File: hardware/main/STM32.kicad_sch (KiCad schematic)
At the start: 36 parts, among them U201 REF3430QDGKRQ1, U202 STM32L431RCTx

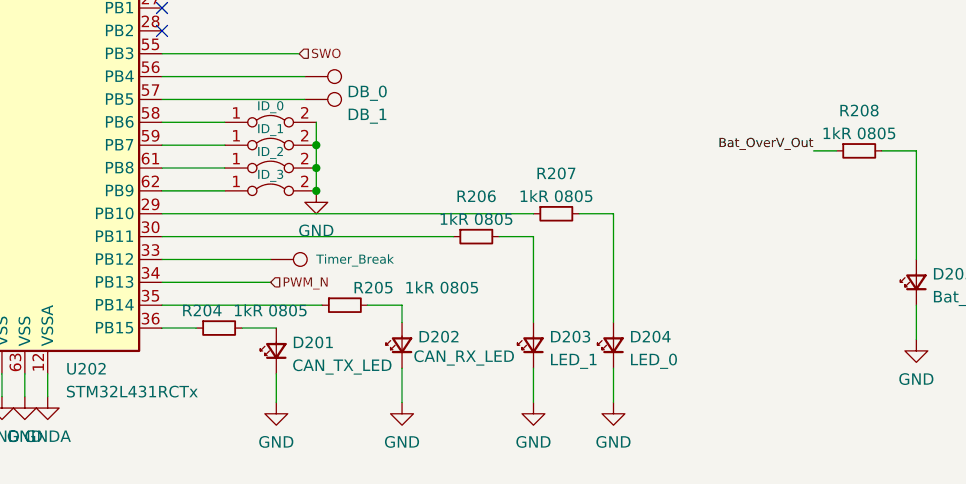
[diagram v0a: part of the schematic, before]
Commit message: Schematics: Change LED order for better pcb routing
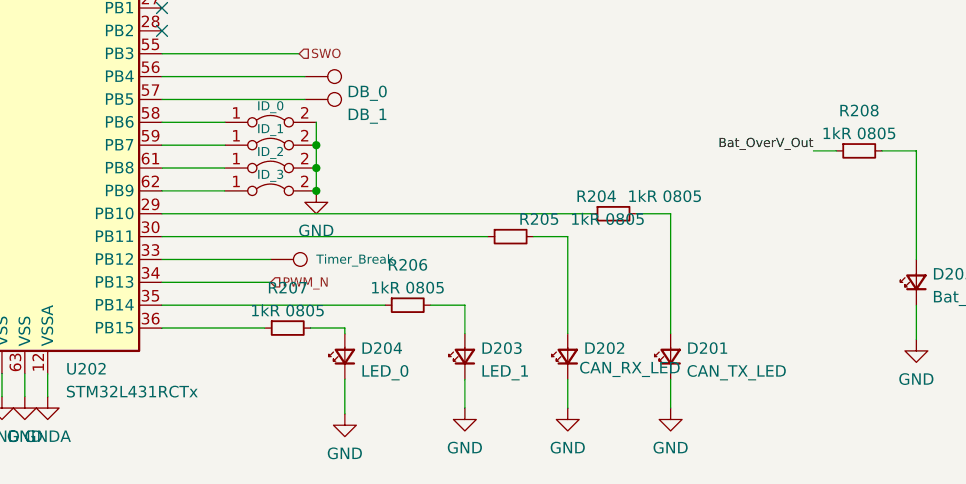
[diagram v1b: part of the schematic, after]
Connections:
- net at R205.1: now also U202.30 (PB11); no longer U202.35 (PB14)
- net at R207.1: now also U202.36 (PB15); no longer U202.29 (PB10)
- net at R206.1: now also U202.35 (PB14); no longer U202.30 (PB11)
- net at R204.1: now also U202.29 (PB10); no longer U202.36 (PB15)
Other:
- moved on the sheet: D201, D202, D203, D204, R204, R205, R206, R207

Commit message: Layout: WIP updating control
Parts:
- removed JP202: Enable Voltage Reference, Zenite:SolderJumper-2_P0.5mm_Open_TrianglePad0.5x0.5mm, symbol Jumper:Jumper_2_Bridged
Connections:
- net 5VA is gone; now on net 5V: C201.2, C202.2, U201.1 (ENABLE), U201.8 (VIN)
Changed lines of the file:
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@@
-    (stroke (width 0) (type default) (color 0 0 0 0))
-  )
-  (wire (pts (xy 246.38 22.86) (xy 250.053 22.86))
     (stroke (width 0) (type default) (color 0 0 0 0))
   )
@@
     (stroke (width 0) (type default) (color 0 0 0 0))
   )
-  (wire (pts (xy 232.41 22.86) (xy 236.22 22.86))
+  (wire (pts (xy 232.41 22.86) (xy 250.053 22.86))
     (stroke (width 0) (type default) (color 0 0 0 0))
   )
@@
     (pin "1")
   )
-  (symbol (lib_id "Jumper:Jumper_2_Bridged") (at 241.3 22.86 0) (unit 1)
-    (in_bom yes) (on_board yes) (fields_autoplaced)
-    (property "Reference" "JP202" (id 0) (at 241.3 18.5252 0))
-    (property "Value" "Enable Voltage Reference" (id 1) (at 241.3 21.0621 0))
-    (property "Footprint" "Zenite:SolderJumper-2_P0.5mm_Open_TrianglePad0.5x0.5mm" (id 2) (at 241.3 22.86 0)
-      (effects (font (size 1.27 1.27)) hide)
-    )
-    (property "Datasheet" "~" (id 3) (at 241.3 22.86 0)
-      (effects (font (size 1.27 1.27)) hide)
-    )
-    (pin "1")
-    (pin "2")
-  )
   (symbol (lib_id "Jumper:Jumper_2_Bridged") (at 240.03 50.165 0) (unit 1)

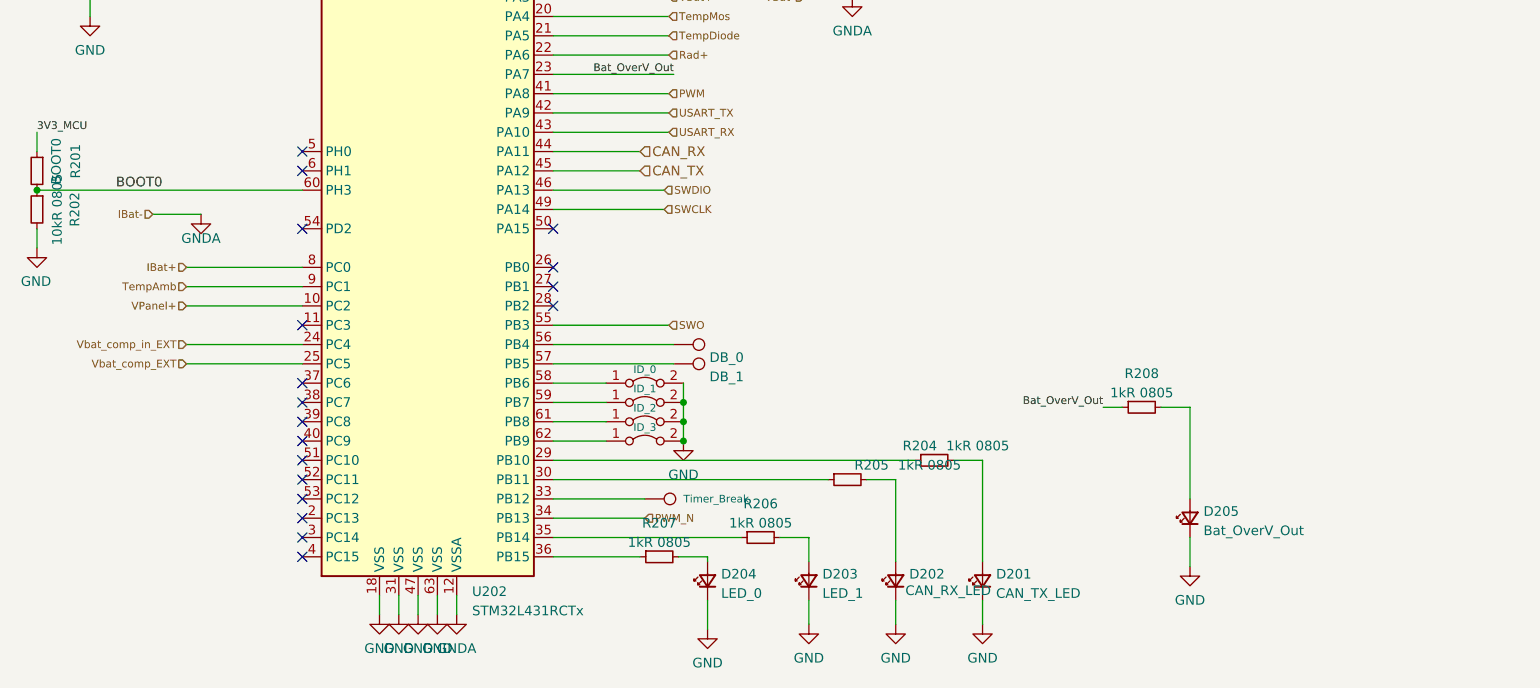
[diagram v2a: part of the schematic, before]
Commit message: Layout: Designing thermal dissipation and optimizing control
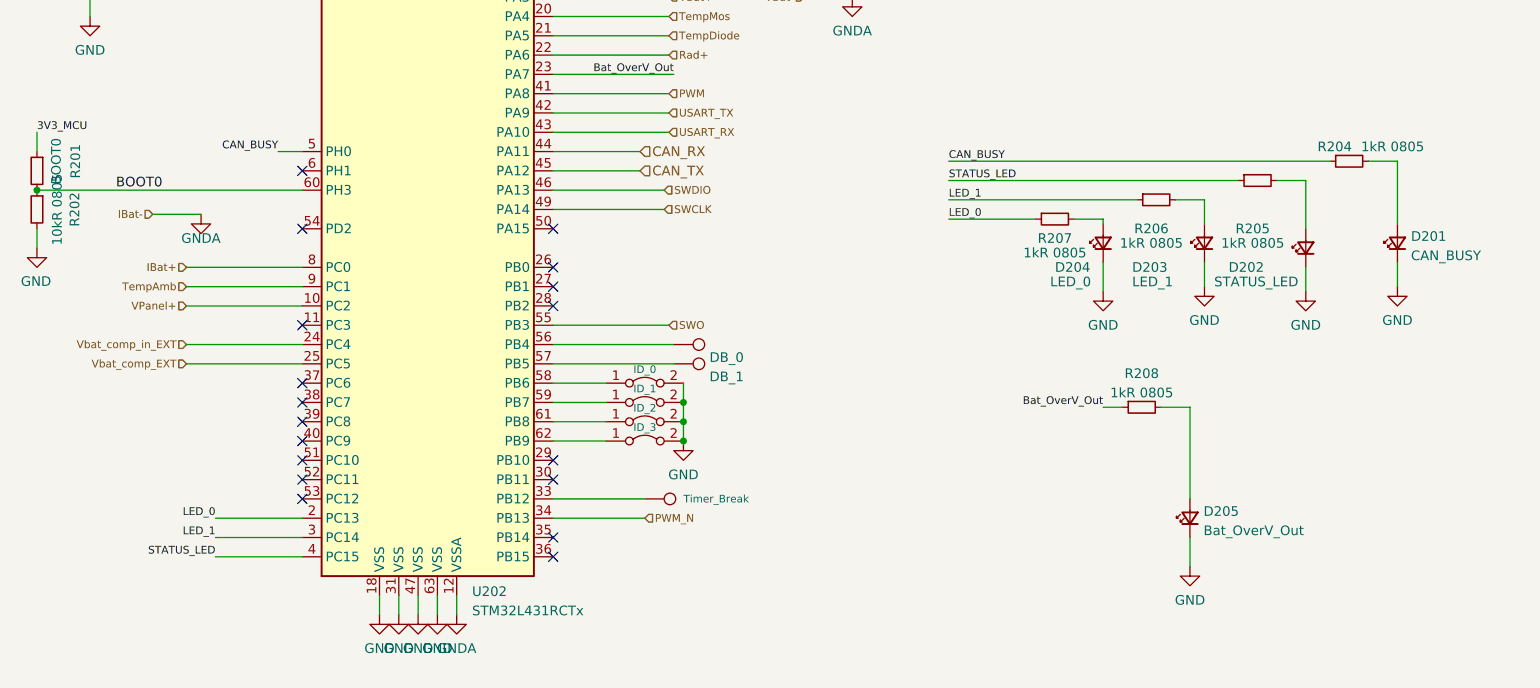
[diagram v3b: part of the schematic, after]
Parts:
- D201: value CAN_TX_LED -> CAN_BUSY
- D202: value CAN_RX_LED -> STATUS_LED
- JP203: footprint Jumper:SolderJumper-3_P2.0mm_Open_TrianglePad1.0x1.5mm -> Zenite:SolderJumper-3_P0.5mm_Open_TrianglePad0.8x0.5mm
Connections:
- net at U202.30 (PB11): no longer R205.1
- net at U202.36 (PB15): no longer R207.1
- net at U202.35 (PB14): no longer R206.1
- net at U202.29 (PB10): no longer R204.1
- net LED_0: now reaches U202.2 (PC13)
- net LED_0: now also R207.1
- net LED_1: now reaches U202.3 (PC14)
- net LED_1: now also R206.1
- net STATUS_LED: now reaches U202.4 (PC15)
- net STATUS_LED: now also R205.1
- net CAN_BUSY: now reaches U202.5 (PH0)
- net CAN_BUSY: now also R204.1
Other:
- moved on the sheet: D201, D202, D203, D204, R204, R205, R206, R207

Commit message: Layout: Connect all unconected nets, and fix all DRC errors
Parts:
- JP201, JP204, JP205, JP206, JP207: footprint Zenite:SolderJumper-2_P0.5mm_Open_TrianglePad0.5x0.5mm -> Zenite:SolderJumper-2_P0.5mm_Open_TrianglePad0.8x0.5mm
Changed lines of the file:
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@@
       (effects (font (size 1 1)))
     )
-    (property "Footprint" "Zenite:SolderJumper-2_P0.5mm_Open_TrianglePad0.5x0.5mm" (id 2) (at 167.64 142.24 0)
+    (property "Footprint" "Zenite:SolderJumper-2_P0.5mm_Open_TrianglePad0.8x0.5mm" (id 2) (at 167.64 142.24 0)
       (effects (font (size 1.27 1.27)) hide)
     )
@@
     (property "Reference" "JP201" (id 0) (at 240.03 45.8302 0))
     (property "Value" "Enable Stm32 Supply" (id 1) (at 240.03 48.3671 0))
-    (property "Footprint" "Zenite:SolderJumper-2_P0.5mm_Open_TrianglePad0.5x0.5mm" (id 2) (at 240.03 50.165 0)
+    (property "Footprint" "Zenite:SolderJumper-2_P0.5mm_Open_TrianglePad0.8x0.5mm" (id 2) (at 240.03 50.165 0)
       (effects (font (size 1.27 1.27)) hide)
     )
@@
       (effects (font (size 1 1)))
     )
-    (property "Footprint" "Zenite:SolderJumper-2_P0.5mm_Open_TrianglePad0.5x0.5mm" (id 2) (at 167.64 137.16 0)
+    (property "Footprint" "Zenite:SolderJumper-2_P0.5mm_Open_TrianglePad0.8x0.5mm" (id 2) (at 167.64 137.16 0)
       (effects (font (size 1.27 1.27)) hide)
     )
@@
       (effects (font (size 1 1)))
     )
-    (property "Footprint" "Zenite:SolderJumper-2_P0.5mm_Open_TrianglePad0.5x0.5mm" (id 2) (at 167.64 139.7 0)
+    (property "Footprint" "Zenite:SolderJumper-2_P0.5mm_Open_TrianglePad0.8x0.5mm" (id 2) (at 167.64 139.7 0)
       (effects (font (size 1.27 1.27)) hide)
     )
@@
       (effects (font (size 1 1)))
     )
-    (property "Footprint" "Zenite:SolderJumper-2_P0.5mm_Open_TrianglePad0.5x0.5mm" (id 2) (at 167.64 134.62 0)
-      (effects (font (size 1.27 1.27)) hide)
-    )
+    (property "Footprint" "Zenite:SolderJumper-2_P0.5mm_Open_TrianglePad0.8x0.5mm" (id 2) (at 167.64 134.62 0)
+      (effects (font (size 1.27 1.27)) hide)
+    )

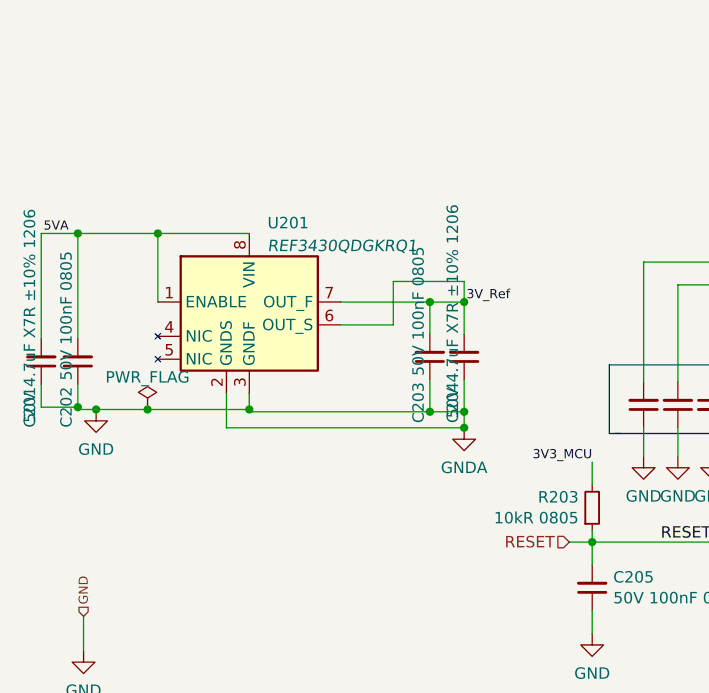
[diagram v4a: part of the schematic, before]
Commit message: layout: Separating analogical power nets
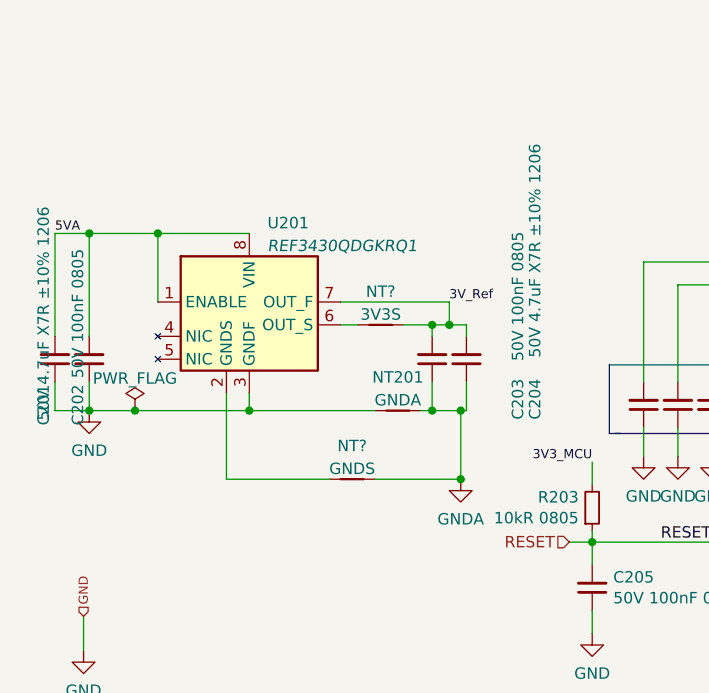
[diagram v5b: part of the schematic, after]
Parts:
- added NT201: GNDA, Resistor_SMD:R_0201_0603Metric, symbol Device:NetTie_2
- added NT?: 3V3S, Resistor_SMD:R_0201_0603Metric, symbol Device:NetTie_2
- added NT?: GNDS, Resistor_SMD:R_0201_0603Metric, symbol Device:NetTie_2
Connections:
- net 3V_Ref: now also NT?.1; no longer U201.6 (OUT_S)
- net GND: now also NT201.2; no longer C203.1, C204.1, C211.1, U201.2 (GNDS), U202.12 (VSSA), U202.15 (PA1)
- new net: NT?.2, U201.6 (OUT_S)
- new net: NT?.2, U201.2 (GNDS)
- new net GNDA: C203.1, C204.1, C211.1, NT201.1, NT?.1, U202.12 (VSSA), U202.15 (PA1)
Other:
- moved on the sheet: C201, C202

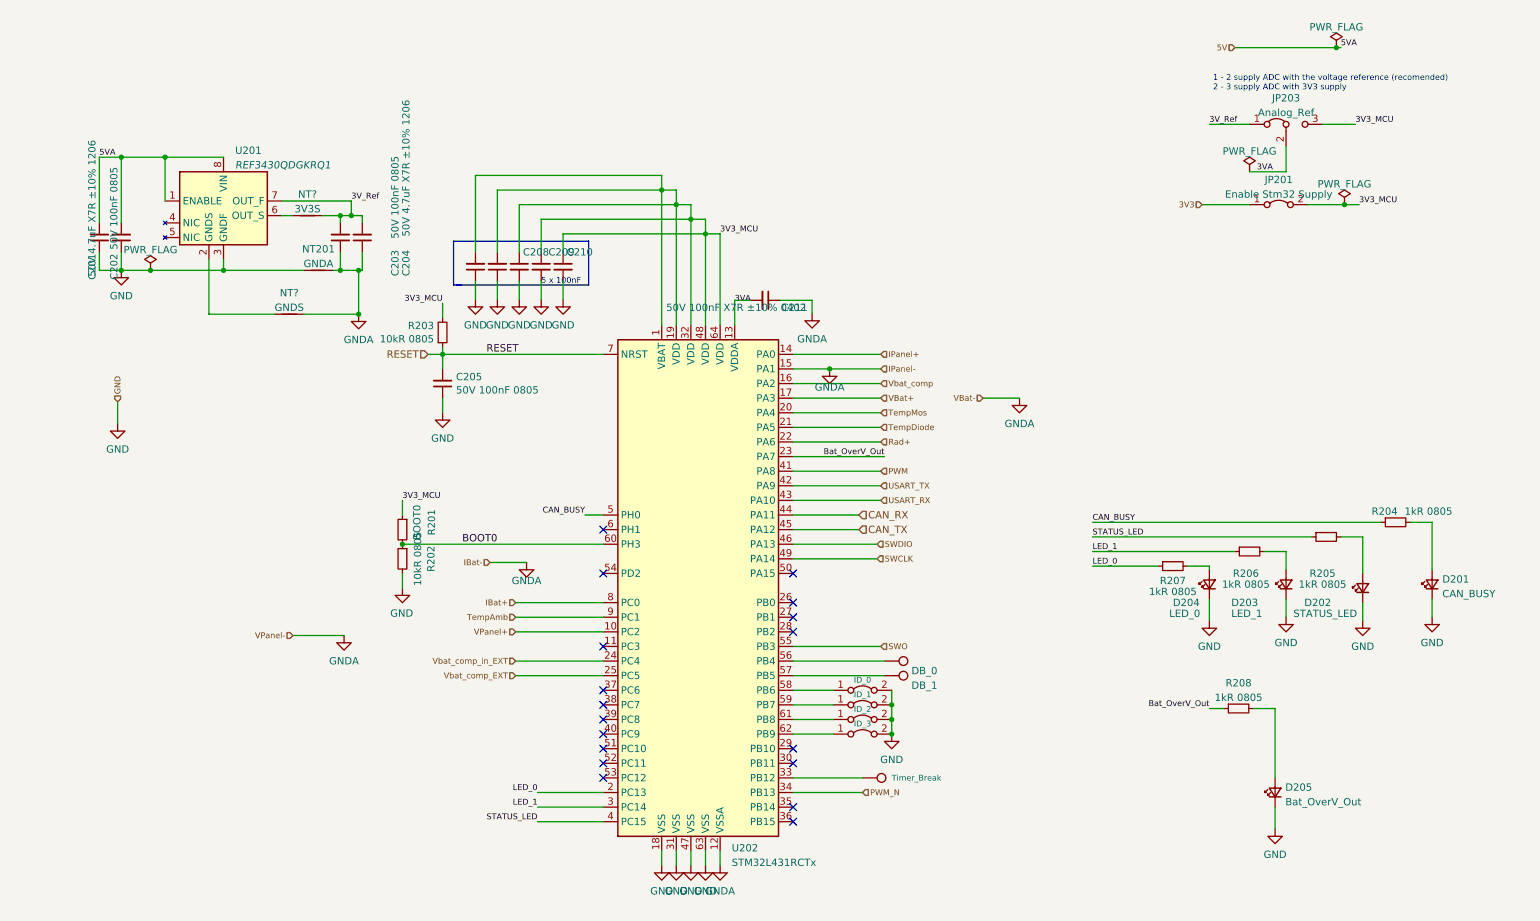
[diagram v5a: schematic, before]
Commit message: Layout: Place components and route analog, supplies and CAN
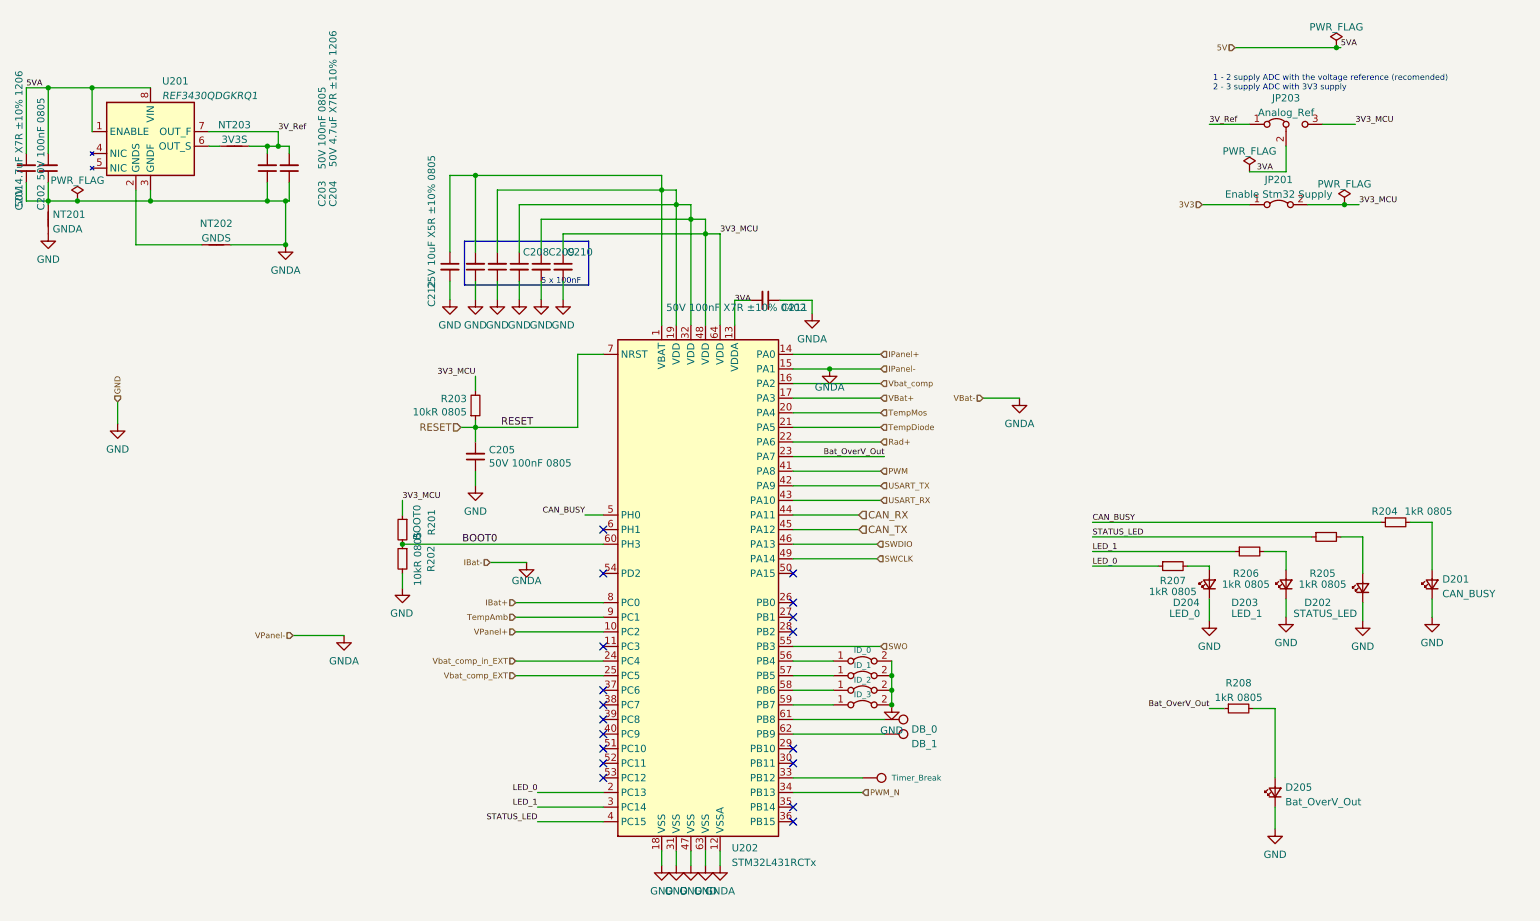
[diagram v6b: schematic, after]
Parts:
- added C212: 25V 10uF X5R ±10% 0805, Capacitor_SMD:C_0805_2012Metric_Pad1.18x1.45mm_HandSolder, symbol Device:C_Small
- TP201, TP202: footprint TestPoint:TestPoint_Pad_2.0x2.0mm -> TestPoint:TestPoint_Pad_1.5x1.5mm
- TP203: footprint TestPoint:TestPoint_Pad_2.0x2.0mm -> TestPoint:TestPoint_Pad_1.0x1.0mm
- gave numbers to parts that had none: 2
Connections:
- net 3V3_MCU: now also C212.1
- net GND: now also C212.2; no longer C201.1, C202.1, U201.3 (GNDF)
- net GNDA: now also C201.1, C202.1, U201.3 (GNDF)
- net at TP201.1: now also U202.61 (PB8); no longer U202.56 (PB4)
- net at JP207.1 (A): now also U202.59 (PB7); no longer U202.62 (PB9)
- net at TP202.1: now also U202.62 (PB9); no longer U202.57 (PB5)
- net at JP204.1 (A): now also U202.56 (PB4); no longer U202.58 (PB6)
- net at JP205.1 (A): now also U202.57 (PB5); no longer U202.59 (PB7)
- net at JP206.1 (A): now also U202.58 (PB6); no longer U202.61 (PB8)
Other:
- moved on the sheet: C201, C202, C203, C204, C205, NT201, NT202, NT203, R203, U201
